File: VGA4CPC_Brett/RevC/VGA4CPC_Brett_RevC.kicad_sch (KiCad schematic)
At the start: 49 parts, among them J1 CPC VIDEO IN, J2 LUM OUT, J3 +5V IN, J4 VFREQ, J5 SPARE GPIO, J6 VGA OUT, SW1 RESET, SW2 WACKED, U1 RASPBERRY PI PICO2, U2 74LVC245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

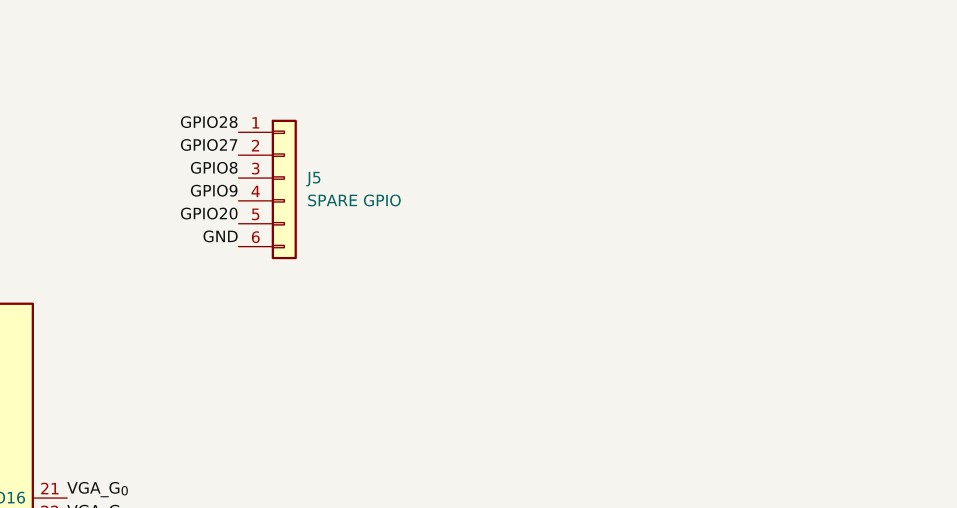
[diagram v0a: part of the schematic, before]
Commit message: Added +3.3V on spare GPIO header
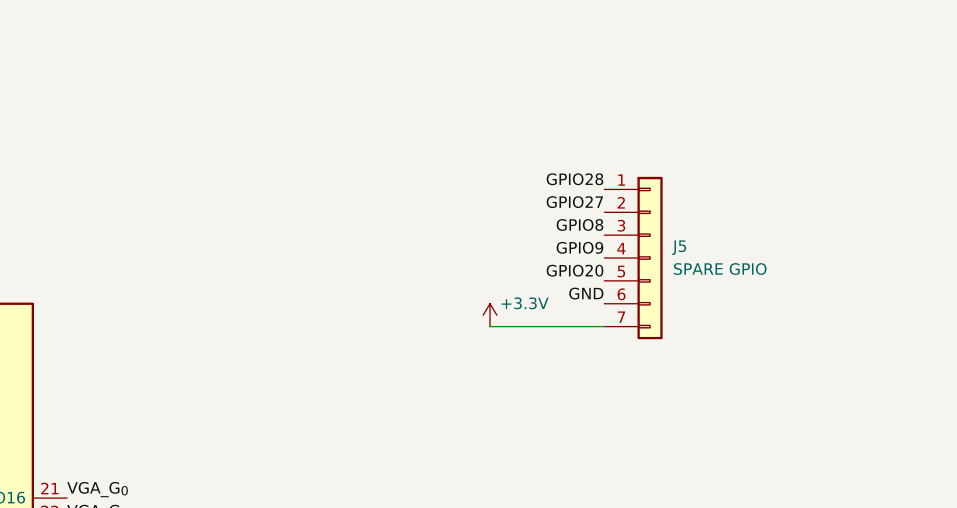
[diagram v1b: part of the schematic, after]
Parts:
- removed J5: SPARE GPIO, Connector_PinHeader_2.54mm:PinHeader_1x06_P2.54mm_Vertical, symbol Connector_Generic:Conn_01x06
- added J5: SPARE GPIO, Connector_PinHeader_2.54mm:PinHeader_1x07_P2.54mm_Vertical, symbol Connector_Generic:Conn_01x07
- U1: footprint Package_SO:SOIC-20W_7.5x12.8mm_P1.27mm -> Module:RaspberryPi_Pico_Common_Unspecified
- U2: footprint Module:RaspberryPi_Pico_Common_Unspecified -> Package_SO:SOIC-20W_7.5x12.8mm_P1.27mm
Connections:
- net +3.3V: now also J5.7 (Pin_7)
- net GND: now also J5.6 (Pin_6)
- net GPIO20: now also J5.5 (Pin_5)
- net GPIO27: now also J5.2 (Pin_2)
- net GPIO28: now also J5.1 (Pin_1)
- net GPIO8: now also J5.3 (Pin_3)
- net GPIO9: now also J5.4 (Pin_4)
